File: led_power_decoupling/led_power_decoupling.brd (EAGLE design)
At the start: 100 x 80 mm, 0 parts

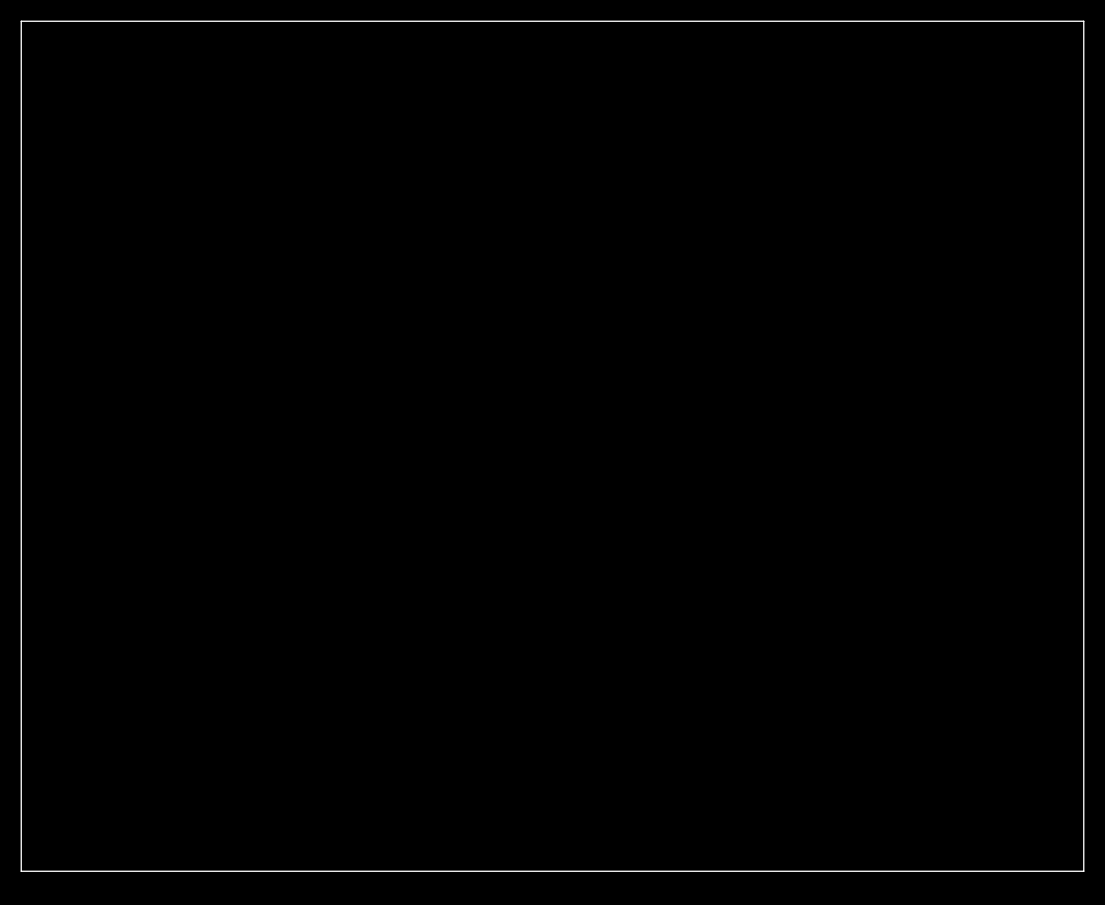
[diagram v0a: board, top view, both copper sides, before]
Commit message: LED power decoupling board
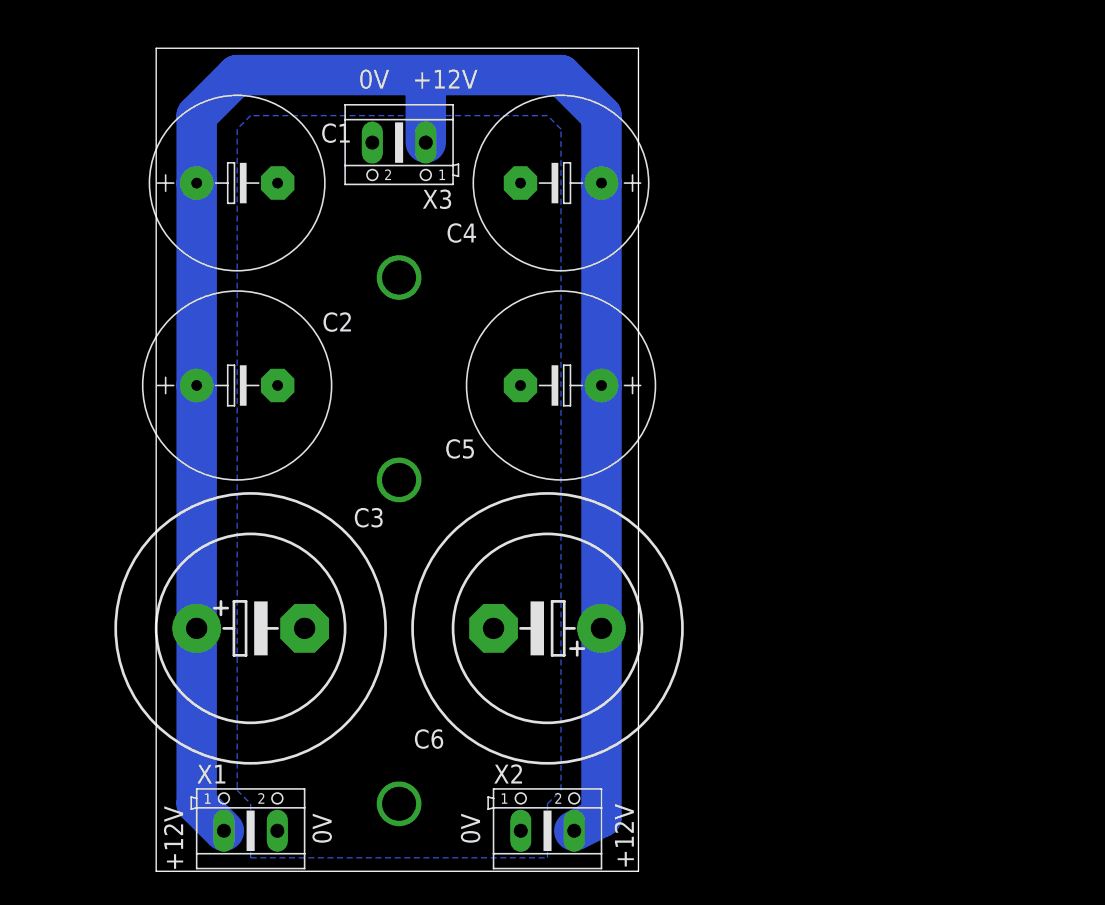
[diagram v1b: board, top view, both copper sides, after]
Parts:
- added C1, C4: 10mF, rcl:E7,5-16
- added C2, C5: 10mF (low. imp.), rcl:E7,5-18
- added C3, C6: 22mF, rcl:EB25D
- added X1: out 1, con-ptr500:AK500/2
- added X2: out 2, con-ptr500:AK500/2
- added X3: input, con-ptr500:AK500/2
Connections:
- new net +12V: C1.+, C2.+, C3.+, C4.+, C5.+, C6.+, X1.1, X2.2, X3.1
- new net 0V: C1.-, C2.-, C3.-, C4.-, C5.-, C6.-, X1.2, X2.1, X3.2
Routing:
- net +12V: track 0.00 -> 184.9 mm
- added copper zone on layer 16, net 0V
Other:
- board size 100 x 80 mm -> 45.4 x 77.5 mm
- board text added: "+12V"
- board text added: "0V"
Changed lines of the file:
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@@
 <layer number="43" name="vRestrict" color="2" fill="10" visible="yes" active="yes"/>
 <layer number="44" name="Drills" color="7" fill="1" visible="no" active="yes"/>
-<layer number="45" name="Holes" color="7" fill="1" visible="no" active="yes"/>
+<layer number="45" name="Holes" color="7" fill="1" visible="yes" active="yes"/>
 <layer number="46" name="Milling" color="3" fill="1" visible="no" active="yes"/>
 <layer number="47" name="Measures" color="7" fill="1" visible="no" active="yes"/>
@@
 <board>
 <plain>
-<wire x1="0" y1="0" x2="100" y2="0" width="0" layer="20"/>
-<wire x1="100" y1="0" x2="100" y2="80" width="0" layer="20"/>
-<wire x1="100" y1="80" x2="0" y2="80" width="0" layer="20"/>
-<wire x1="0" y1="80" x2="0" y2="0" width="0" layer="20"/>
+<wire x1="12.7" y1="0" x2="58.09" y2="0" width="0" layer="20"/>
+<wire x1="58.09" y1="0" x2="58.09" y2="77.46" width="0" layer="20"/>
+<wire x1="58.09" y1="77.46" x2="12.7" y2="77.46" width="0" layer="20"/>
+<wire x1="12.7" y1="77.46" x2="12.7" y2="0" width="0" layer="20"/>
+<text x="15.24" y="0" size="1.778" layer="25" rot="R90">+12V</text>
+<text x="55.88" y="6.35" size="1.778" layer="25" rot="R270">+12V</text>
+<text x="36.83" y="73.66" size="1.778" layer="25">+12V</text>
+<text x="31.75" y="73.66" size="1.778" layer="25">0V</text>
+<text x="29.21" y="2.54" size="1.778" layer="25" rot="R90">0V</text>
+<text x="43.18" y="2.54" size="1.778" layer="25" rot="R90">0V</text>
 </plain>
 <attributes>
@@
 </autorouter>
 <elements>
+<element name="C1" library="rcl" package="E7,5-16" value="10mF" x="20.32" y="64.77"/>
+<element name="C2" library="rcl" package="E7,5-18" value="10mF (low. imp.)" x="20.32" y="45.72"/>
+<element name="C3" library="rcl" package="EB25D" value="22mF" x="21.59" y="22.86"/>
+<element name="X1" library="con-ptr500" package="AK500/2" value="out 1" x="21.59" y="3.81" smashed="yes">
+<attribute name="OC_FARNELL" value="unknown" x="21.59" y="3.81" size="1.778" layer="27" display="off"/>
+<attribute name="MPN" value="" x="21.59" y="3.81" size="1.778" layer="27" display="off"/>
+<attribute name="OC_NEWARK" value="unknown" x="21.59" y="3.81" size="1.778" layer="27" display="off"/>
+<attribute name="MF" value="" x="21.59" y="3.81" size="1.778" layer="27" display="off"/>
+<attribute name="NAME" x="16.51" y="8.255" size="1.778" layer="25" ratio="10"/>
+<attribute name="VALUE" x="20.32" y="8.255" size="1.778" layer="27" ratio="10"/>
+</element>
+<element name="C4" library="rcl" package="E7,5-16" value="10mF" x="50.8" y="64.77" rot="R180"/>
+<element name="C5" library="rcl" package="E7,5-18" value="10mF (low. imp.)" x="50.8" y="45.72" rot="R180"/>
+<element name="C6" library="rcl" package="EB25D" value="22mF" x="49.53" y="22.86" rot="R180"/>
+<element name="X2" library="con-ptr500" package="AK500/2" value="out 2" x="49.53" y="3.81" smashed="yes">
+<attribute name="OC_FARNELL" value="unknown" x="8.89" y="-27.94" size="1.778" layer="27" display="off"/>
+<attribute name="MPN" value="" x="8.89" y="-27.94" size="1.778" layer="27" display="off"/>
+<attribute name="OC_NEWARK" value="unknown" x="8.89" y="-27.94" size="1.778" layer="27" display="off"/>
+<attribute name="MF" value="" x="8.89" y="-27.94" size="1.778" layer="27" display="off"/>
+<attribute name="NAME" x="44.45" y="8.255" size="1.778" layer="25" ratio="10"/>
+<attribute name="VALUE" x="48.26" y="8.255" size="1.778" layer="27" ratio="10"/>
+</element>
+<element name="X3" library="con-ptr500" package="AK500/2" value="input" x="35.56" y="68.58" smashed="yes" rot="R180">
+<attribute name="OC_FARNELL" value="unknown" x="35.56" y="68.58" size="1.778" layer="27" rot="R180" display="off"/>
+<attribute name="MPN" value="" x="35.56" y="68.58" size="1.778" layer="27" rot="R180" display="off"/>
+<attribute name="OC_NEWARK" value="unknown" x="35.56" y="68.58" size="1.778" layer="27" rot="R180" display="off"/>
+<attribute name="MF" value="" x="35.56" y="68.58" size="1.778" layer="27" rot="R180" display="off"/>
+<attribute name="NAME" x="40.64" y="64.135" size="1.778" layer="25" ratio="10" rot="R180"/>
+<attribute name="VALUE" x="35.56" y="64.135" size="1.778" layer="27" ratio="10" rot="R180"/>
+</element>
 </elements>
 <signals>
+<signal name="0V">
+<contactref element="X1" pad="2"/>
+<contactref element="C1" pad="-"/>
+<contactref element="C2" pad="-"/>
+<contactref element="C3" pad="-"/>
+<contactref element="C4" pad="-"/>
+<contactref element="C5" pad="-"/>
+<contactref element="C6" pad="-"/>
+<contactref element="X2" pad="1"/>
+<contactref element="X3" pad="2"/>
+<polygon width="0.4064" layer="16" isolate="1.016">
+<vertex x="49.53" y="71.12"/>
+<vertex x="21.59" y="71.12"/>
+<vertex x="20.32" y="69.85"/>
+<vertex x="20.32" y="7.62"/>
+<vertex x="21.59" y="6.35"/>
+<vertex x="21.59" y="1.27"/>
+<vertex x="49.53" y="1.27"/>
+<vertex x="49.53" y="6.35"/>
+<vertex x="50.8" y="7.62"/>
+<vertex x="50.8" y="69.85"/>
+</polygon>
+</signal>
+<signal name="+12V">
+<contactref element="X1" pad="1"/>
+<contactref element="C1" pad="+"/>
+<contactref element="C2" pad="+"/>
+<contactref element="C3" pad="+"/>
+<contactref element="C4" pad="+"/>
+<contactref element="C5" pad="+"/>
+<contactref element="C6" pad="+"/>
+<contactref element="X2" pad="2"/>
+<contactref element="X3" pad="1"/>
+<wire x1="38.0746" y1="68.58" x2="38.0746" y2="73.6346" width="3.81" layer="16"/>
+<wire x1="38.0746" y1="73.6346" x2="38.1" y2="74.93" width="2.54" layer="16"/>
+<wire x1="38.1" y1="74.93" x2="20.32" y2="74.93" width="3.81" layer="16"/>
+<wire x1="20.32" y1="74.93" x2="16.51" y2="71.12" width="3.81" layer="16"/>
+<wire x1="16.51" y1="71.12" x2="16.51" y2="64.77" width="3.81" layer="16"/>
+<wire x1="16.51" y1="64.77" x2="16.51" y2="45.72" width="3.81" layer="16"/>
+<wire x1="16.51" y1="45.72" x2="16.51" y2="22.86" width="3.81" layer="16"/>
+<wire x1="16.51" y1="22.86" x2="16.51" y2="6.3754" width="3.81" layer="16"/>
+<wire x1="16.51" y1="6.3754" x2="19.0754" y2="3.81" width="3.81" layer="16"/>
+<wire x1="54.61" y1="64.77" x2="54.61" y2="71.12" width="3.81" layer="16"/>
+<wire x1="54.61" y1="71.12" x2="50.8" y2="74.93" width="3.81" layer="16"/>
+<wire x1="50.8" y1="74.93" x2="38.1" y2="74.93" width="3.81" layer="16"/>
+<wire x1="54.61" y1="64.77" x2="54.61" y2="45.72" width="3.81" layer="16"/>
+<wire x1="54.61" y1="45.72" x2="54.61" y2="22.86" width="3.81" layer="16"/>
+<wire x1="54.61" y1="22.86" x2="54.61" y2="5.1054" width="3.81" layer="16"/>
+<wire x1="54.61" y1="5.1054" x2="52.0446" y2="3.81" width="3.81" layer="16"/>
+</signal>
+<signal name="N$1">
+<via x="35.56" y="55.88" extent="1-16" drill="3.2"/>
+</signal>
+<signal name="N$2">
+<via x="35.56" y="6.35" extent="1-16" drill="3.2"/>
+</signal>
+<signal name="N$3">
+<via x="35.56" y="36.83" extent="1-16" drill="3.2"/>
+</signal>
 </signals>
 </board>
